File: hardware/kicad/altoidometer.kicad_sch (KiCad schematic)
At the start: 15 parts, among them U1 DOIT-ESP32-DEVKIT-V1, U3 MAX44248ASA+

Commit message: continued work on circuit schematic again
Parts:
- added J1: Conn_01x15_Pin, symbol Connector:Conn_01x15_Pin
- added J2, J3: AudioJack3, symbol Connector_Audio:AudioJack3
- added SW1, SW2, SW3, SW4, SW5, SW6, SW7, SW8: SW_Push, symbol Switch:SW_Push
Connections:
- net 3V3: now also J1.14 (Pin_14)
- net GND: now also J1.15 (Pin_15), J2.S, J3.S, SW1.1, SW2.2, SW3.1, SW4.2, SW5.2, SW6.1, SW7.1, SW8.2
- net PROBE1: now also J2.T
- net PROBE2: now also J2.R
- net GPIO34: now reaches D1.2 (A), D3.1 (K), R5.1, U1.4 (GPIO34_ADC1-CH6_RTC-GPIO4)
- net GPIO35: now reaches D2.2 (A), D4.1 (K), R6.1, U1.5 (GPIO35_ADC1-CH7_RTC-GPIO5)
- net GPIO27: now reaches U1.10 (GPIO27_ADC2-CH7_RTC-GPIO17), U2.14 (T_IRQ)
- net GPIO0: now reaches U1.23 (GPIO0_ADC2-CH1_RTC-GPIO11)
- net GPIO0: now also J1.8 (Pin_8)
- net GPIO15: now reaches U1.24 (GPIO15_ADC2-CH3_HSPI-CS0_RTC-GPIO13), U2.11 (T_CS)
- net GPIO2: now reaches U1.25 (GPIO2_ADC2-CH2_RTC-GPIO12), U2.5 (DC)
- net GPIO4: now reaches U1.26 (GPIO4_ADC2-CH0_RTC-GPIO10), U2.4 (RESET)
- net GPIO5: now reaches U1.29 (GPIO5_VSPI-CS0), U2.3 (CS)
- net GPIO18: now reaches U1.30 (GPIO18_VSPI-CLK), U2.10 (T_CLK), U2.7 (SCK)
- net GPIO18: now also J1.11 (Pin_11)
- net GPIO19: now reaches U1.31 (GPIO19_VSPI-MISO), U2.13 (T_DO), U2.9 (MISO)
- net GPIO19: now also J1.9 (Pin_9)
- net GPIO21: now reaches U1.32 (GPIO21_I2C-SDA)
- net GPIO21: now also J1.13 (Pin_13)
- net GPIO22: now reaches U1.35 (GPIO22_I2C-SCL)
- net GPIO22: now also J1.12 (Pin_12)
- net GPIO23: now reaches U1.36 (GPIO23_VSPI-MOSI), U2.12 (T_DIN), U2.6 (MOSI)
- net GPIO23: now also J1.10 (Pin_10)
- net at U1.8 (GPIO25_ADC2-CH8_DAC1_RTC-GPIO6): now also J3.R
- net at U1.9 (GPIO26_ADC2-CH9_DAC2_RTC-GPIO7): now also J3.T
- new net GPIO12: J1.7 (Pin_7)
- new net GPIO13: SW1.2
- new net GPIO14: SW4.1
- new net GPIO16: SW3.2
- new net GPIO17: SW2.1
- new net GPIO25: SW5.1
- new net GPIO26: SW6.2
- new net GPIO32: SW7.2
- new net GPIO33: SW8.1
- new net GPIO36: J1.6 (Pin_6)
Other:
- note added: "expansion pins: 1. GND 2. 3V3 3. I2C SDA 4. I2C SCL 5. SPI SCK 6. SPI MOSI 7. SPI MISO 8. SPI CS 9. UART TX 10. UART RX 11. NC 12. NC 13. NC 14. NC 15. NC"
- title: (none) -> Altoidometer
- moved on the sheet: D1, D2, D3, D4, R1, R2, R3, R4, R5, R6, R7, R8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

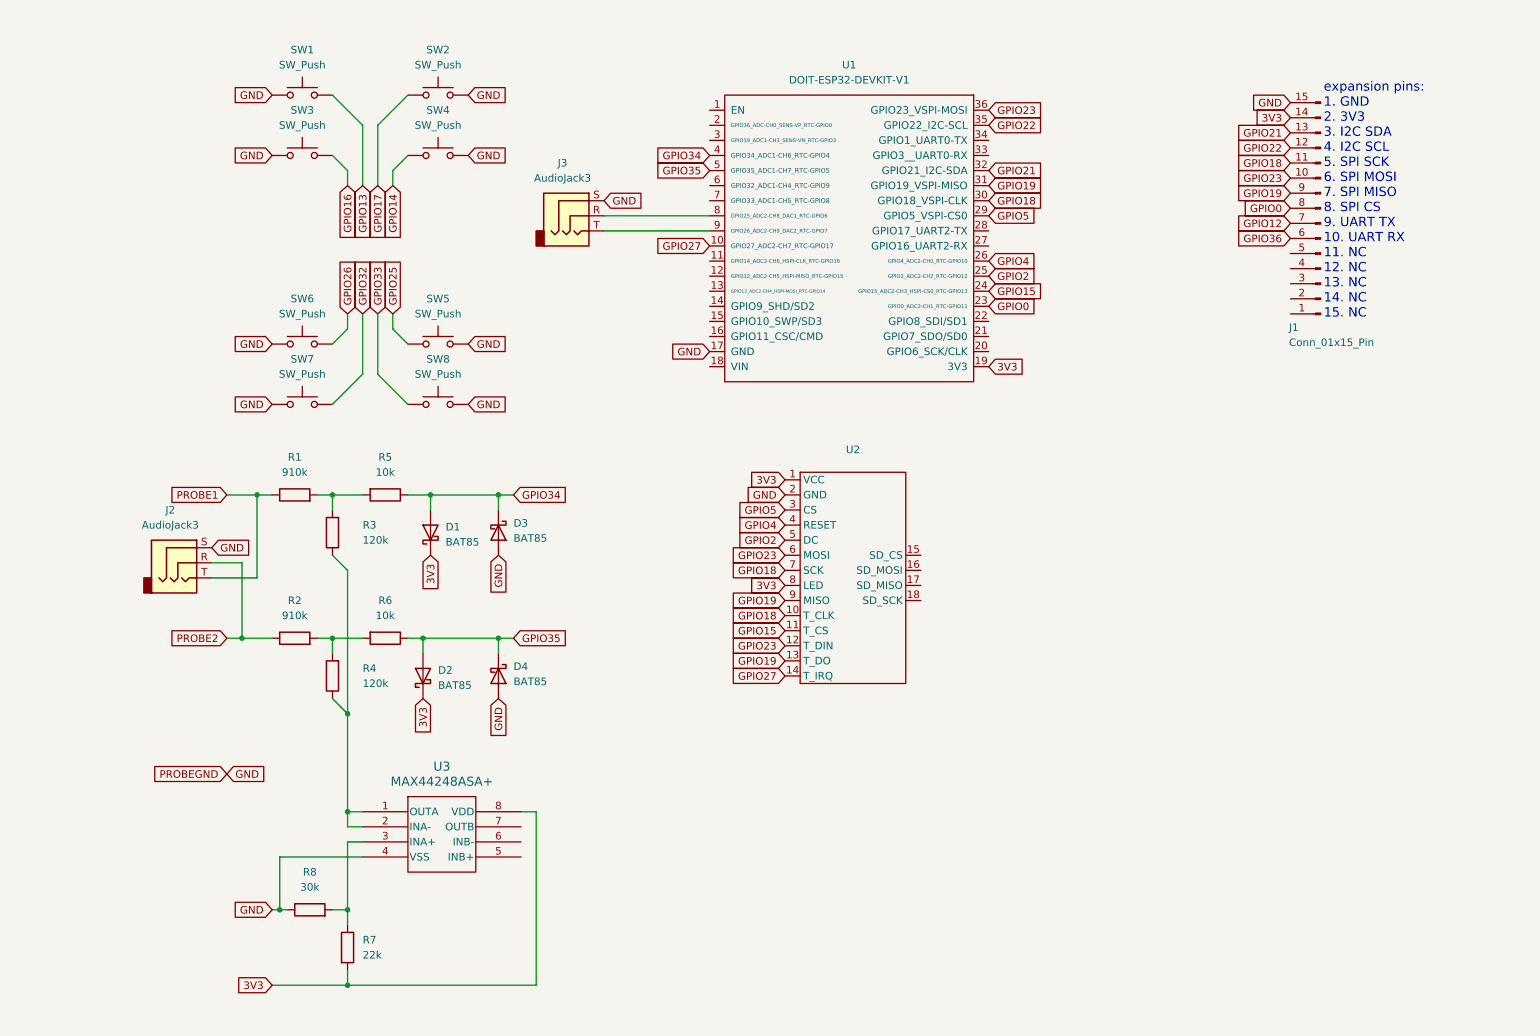
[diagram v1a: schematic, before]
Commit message: changed audio jack configuration and added microsd card module
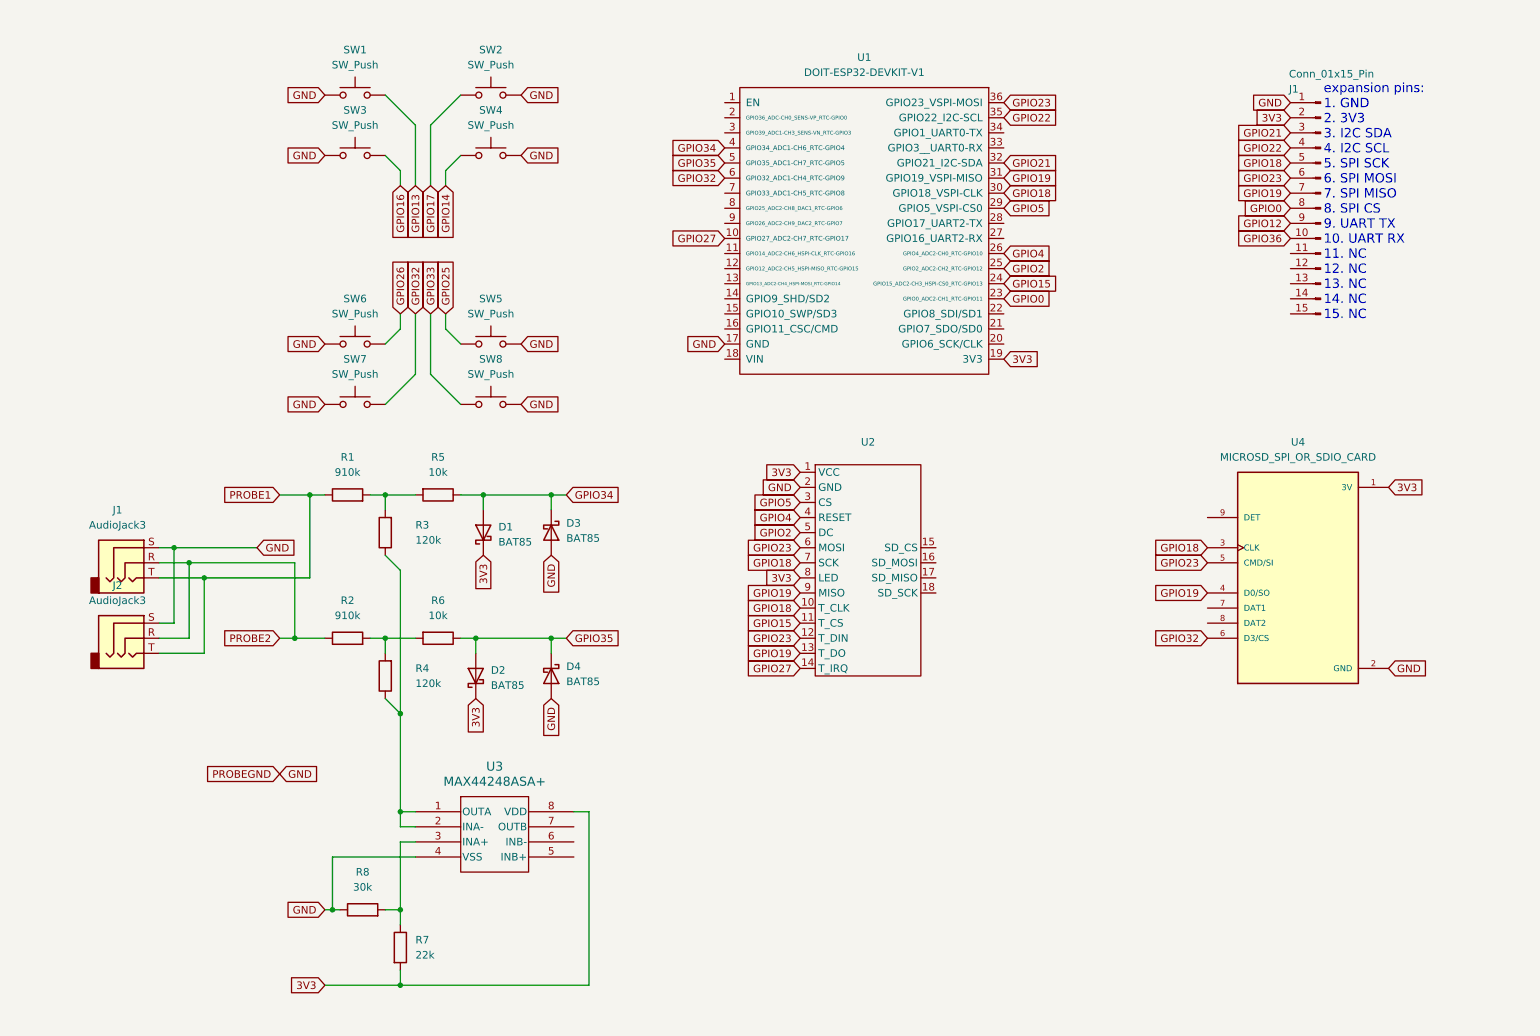
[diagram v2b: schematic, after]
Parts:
- removed J3: AudioJack3, symbol Connector_Audio:AudioJack3
- added J2: AudioJack3, symbol Connector_Audio:AudioJack3
- added U4: MICROSD_SPI_OR_SDIO_CARD, MICROSD_SPI_OR_SDIO_CARD:MODULE_MICROSD_SPI_OR_SDIO_CARD, symbol MICROSD_SPI_OR_SDIO_CARD:MICROSD_SPI_OR_SDIO_CARD
- renumbered J2 to J1
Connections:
- net 3V3: now also J1.2 (Pin_2), U4.1 (3V); no longer J1.14 (Pin_14)
- net GND: now also J1.1 (Pin_1), J2.S, U4.2 (GND); no longer J1.15 (Pin_15)
- net GPIO12: now also J1.9 (Pin_9); no longer J1.7 (Pin_7)
- net GPIO18: now also J1.5 (Pin_5), U4.3 (CLK); no longer J1.11 (Pin_11)
- net GPIO19: now also J1.7 (Pin_7), U4.4 (D0/SO); no longer J1.9 (Pin_9)
- net GPIO21: now also J1.3 (Pin_3); no longer J1.13 (Pin_13)
- net GPIO22: now also J1.4 (Pin_4); no longer J1.12 (Pin_12)
- net GPIO23: now also J1.6 (Pin_6), U4.5 (CMD/SI); no longer J1.10 (Pin_10)
- net GPIO32: now also U1.6 (GPIO32_ADC1-CH4_RTC-GPIO9), U4.6 (D3/CS)
- net GPIO36: now also J1.10 (Pin_10); no longer J1.6 (Pin_6)
- net PROBE1: now also J2.T
- net PROBE2: now also J2.R
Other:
- moved on the sheet: D1, D2, D3, D4, J1, R1, R2, R3, R4, R5, R6, R7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

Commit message: idek kicad just did this when i saved
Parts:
- renumbered J1 to J2
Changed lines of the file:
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@@
 	(title_block
 		(title "Altoidometer")
-		(rev "rev1")
+		(rev "1")
 	)
 	(text "expansion pins:\n1. GND\n2. 3V3\n3. I2C SDA\n4. I2C SCL\n5. SPI SCK\n6. SPI MOSI\n7. SPI MISO\n8. SPI CS\n9. UART TX\n10. UART RX\n11. NC\n12. NC\n13. NC\n14. NC\n15. NC"
@@
 		(on_board yes)
 		(dnp no)
-		(fields_autoplaced yes)
 		(property "Reference" "SW1"
 			(at 71.12 24.13 0)
@@
 		(dnp no)
 		(fields_autoplaced yes)
-		(property "Reference" "J1"
+		(property "Reference" "J2"
 			(at 31.115 101.6 0)
 			(effects
@@
 			(project ""
 				(path "/b57712fc-be2e-4ea6-81e8-e743779dbbdf"
-					(reference "J1")
+					(reference "J2")
 					(unit 1)
 				)

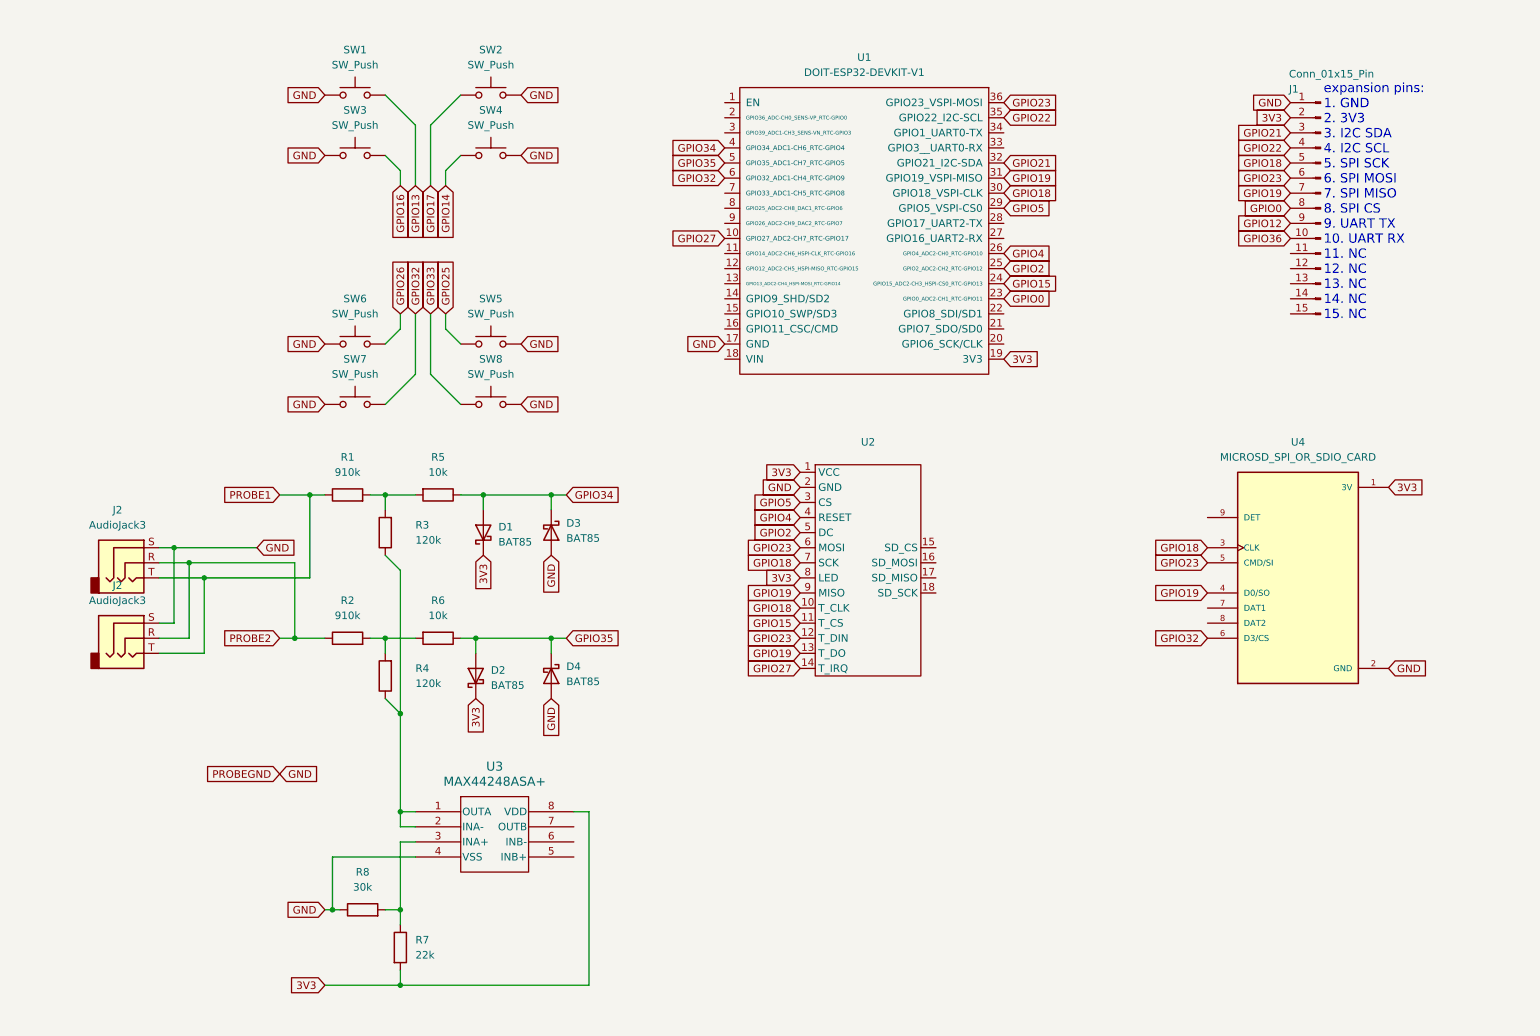
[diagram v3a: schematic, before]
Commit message: Add IMU and GPS modules and update BOM
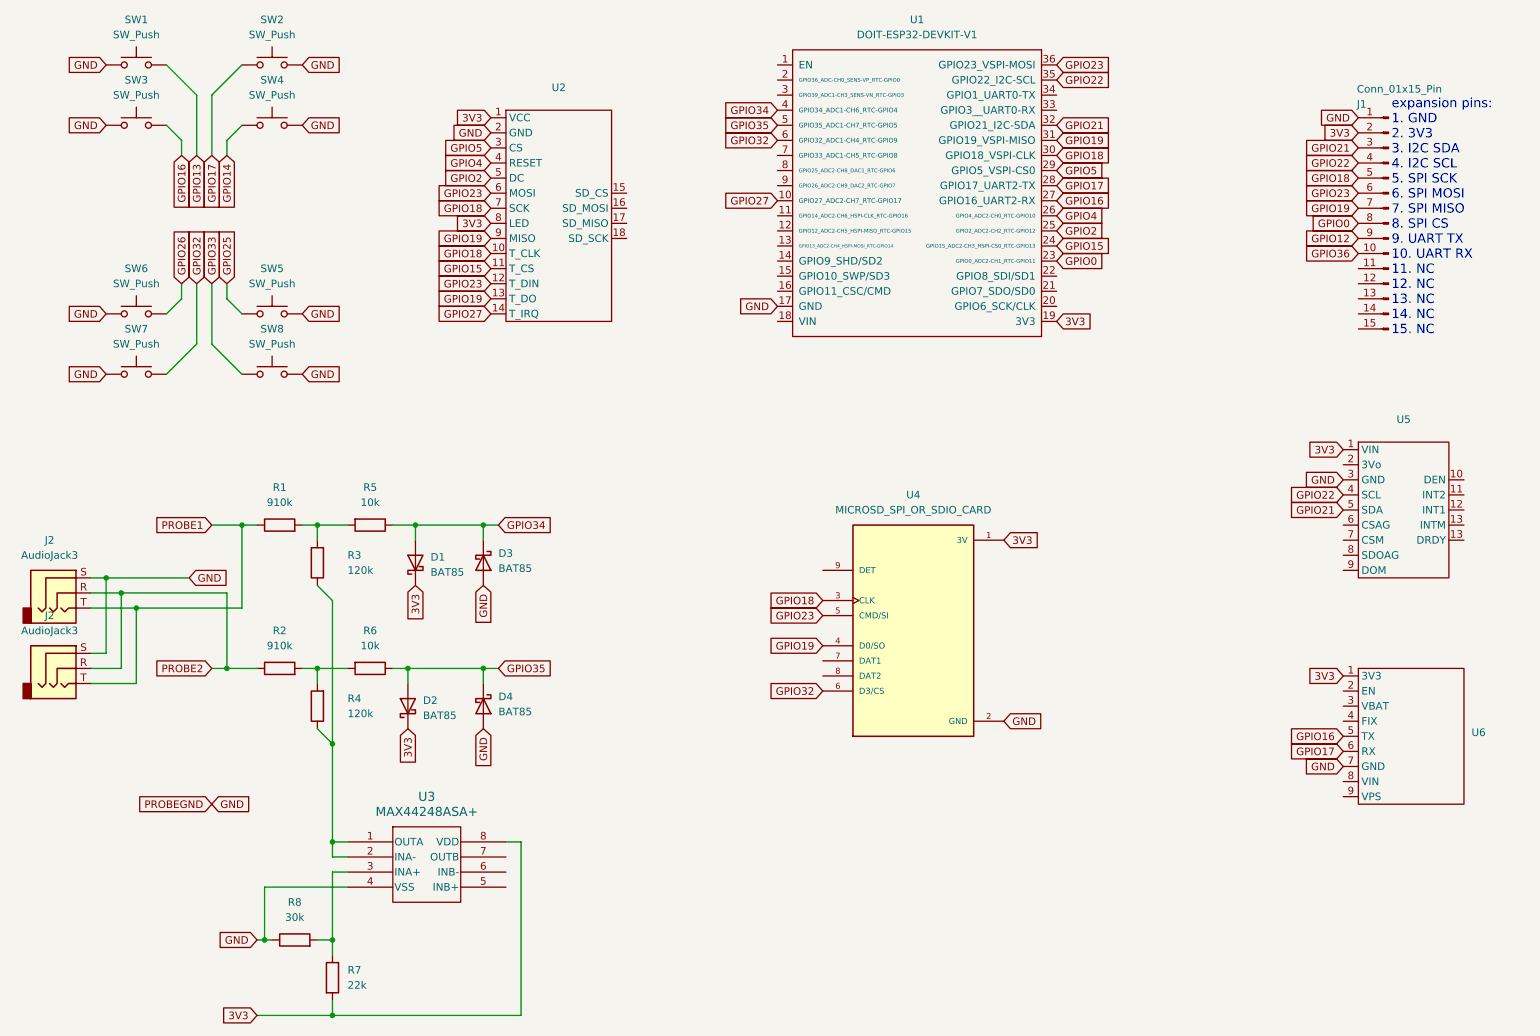
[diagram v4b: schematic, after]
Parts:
- added U5: ~, symbol LSM9DS1_Breakout:LSM9DS1_Breakout
- added U6: ~, symbol ADAFRUIT-5440:ADAFRUIT-5440
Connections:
- net 3V3: now also U5.1 (VIN), U6.1 (3V3)
- net GND: now also U5.3 (GND), U6.7 (GND)
- net GPIO16: now also U1.27 (GPIO16_UART2-RX), U6.5 (TX)
- net GPIO17: now also U1.28 (GPIO17_UART2-TX), U6.6 (RX)
- net GPIO21: now also U5.5 (SDA)
- net GPIO22: now also U5.4 (SCL)
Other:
- moved on the sheet: D1, D2, D3, D4, J1, J2, R1, R2, R3, R4, R5, R6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

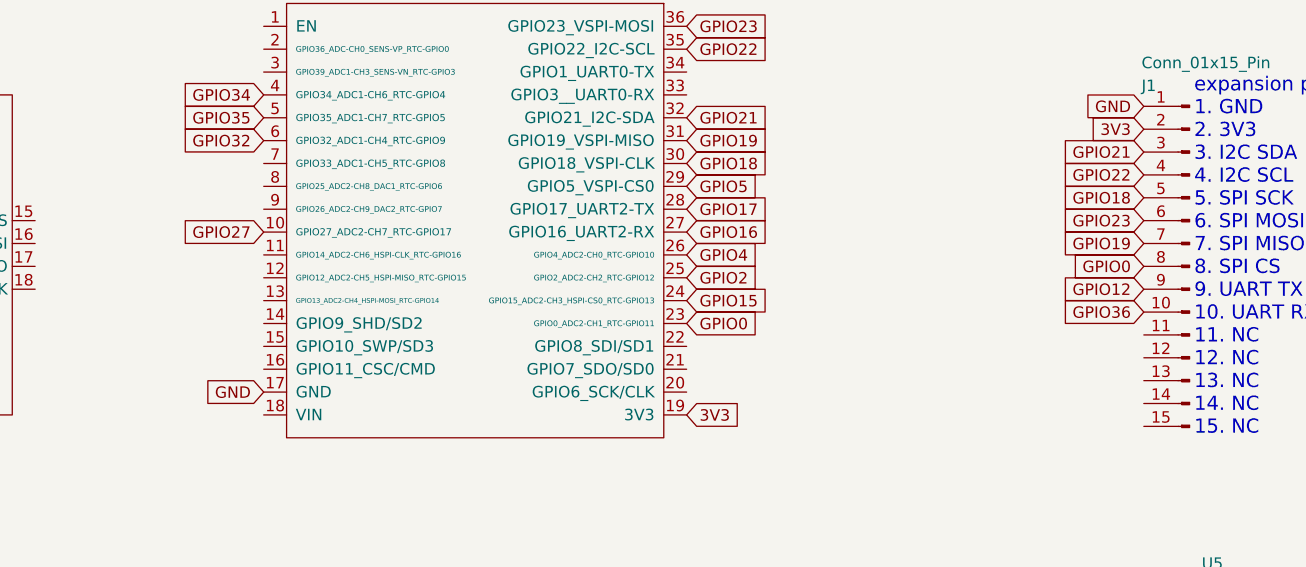
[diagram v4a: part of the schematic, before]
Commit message: Fixed external UART pins
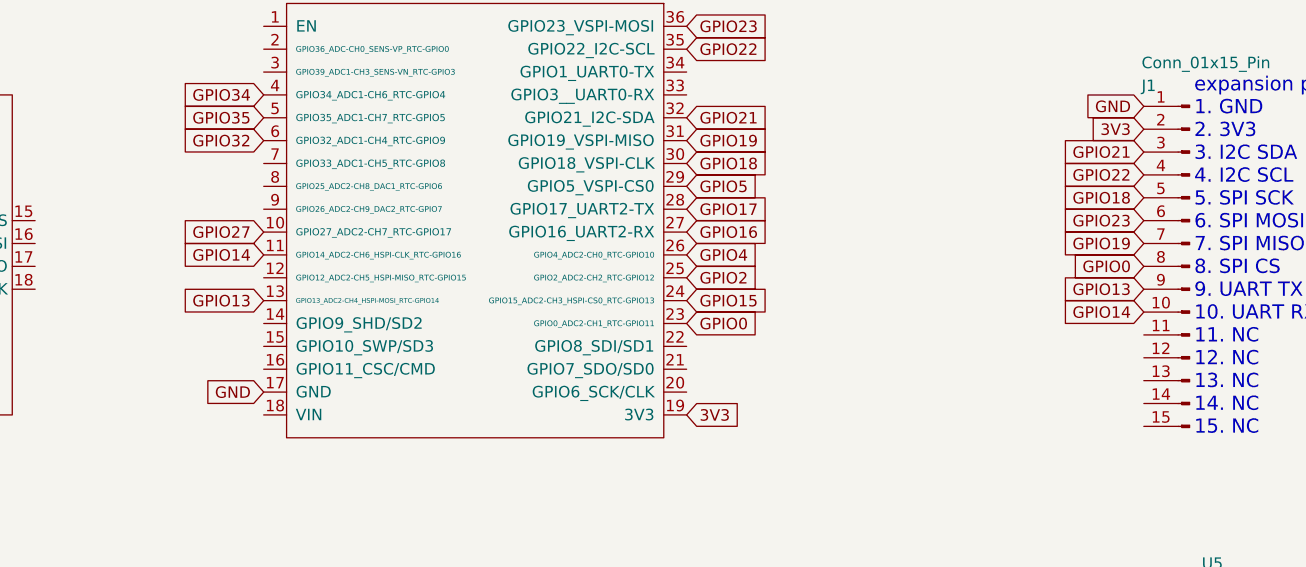
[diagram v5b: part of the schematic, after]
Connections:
- net GPIO12 is gone; now on net GPIO13: J1.9 (Pin_9)
- net GPIO36 is gone; now on net GPIO14: J1.10 (Pin_10)
- net GPIO13: now also U1.13 (GPIO13_ADC2-CH4_HSPI-MOSI_RTC-GPIO14)
- net GPIO14: now also U1.11 (GPIO14_ADC2-CH6_HSPI-CLK_RTC-GPIO16)
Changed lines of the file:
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@@
+		)
+	)
+	(global_label "GPIO13"
+		(shape input)
+		(at 142.24 57.15 180)
+		(fields_autoplaced yes)
+		(effects
+			(font
+				(size 1.27 1.27)
+			)
+			(justify right)
+		)
+		(property "Intersheetrefs" "${INTERSHEET_REFS}"
+			(at 132.3605 57.15 0)
+			(effects
+				(font
+					(size 1.27 1.27)
+				)
+				(justify right)
+				(hide yes)
+			)
 		)
 	)
@@
 		)
 	)
-	(global_label "GPIO36"
+	(global_label "GPIO14"
 		(shape input)
 		(at 240.03 58.42 180)
@@
 		)
 	)
+	(global_label "GPIO14"
+		(shape input)
+		(at 142.24 52.07 180)
+		(fields_autoplaced yes)
+		(effects
+			(font
+				(size 1.27 1.27)
+			)
+			(justify right)
+		)
+		(property "Intersheetrefs" "${INTERSHEET_REFS}"
+			(at 132.3605 52.07 0)
+			(effects
+				(font
+					(size 1.27 1.27)
+				)
+				(justify right)
+				(hide yes)
+			)
+		)
+	)
 	(global_label "GPIO19"
 		(shape input)
@@
 		)
 	)
-	(global_label "GPIO12"
+	(global_label "GPIO13"
 		(shape input)
 		(at 240.03 55.88 180)
